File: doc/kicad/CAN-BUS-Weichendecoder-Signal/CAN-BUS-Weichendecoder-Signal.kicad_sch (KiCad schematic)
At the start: 26 parts, among them J1 Conn_01x04_Male, J1001 Wago 250-1406, J11 250-1406, J12 Wago 250-1406, J13 Wago 250-1406, J14 Wago 250-1406, J15 Wago 250-1406, J21 Conn_01x06, J22 Conn_01x06, U1 PCF8574, U2 PCF8574, U3 PCF8574, U4 PCF8574, U5 ULN2803A, U6 ULN2803A, U7 ULN2803A, U8 ULN2803A

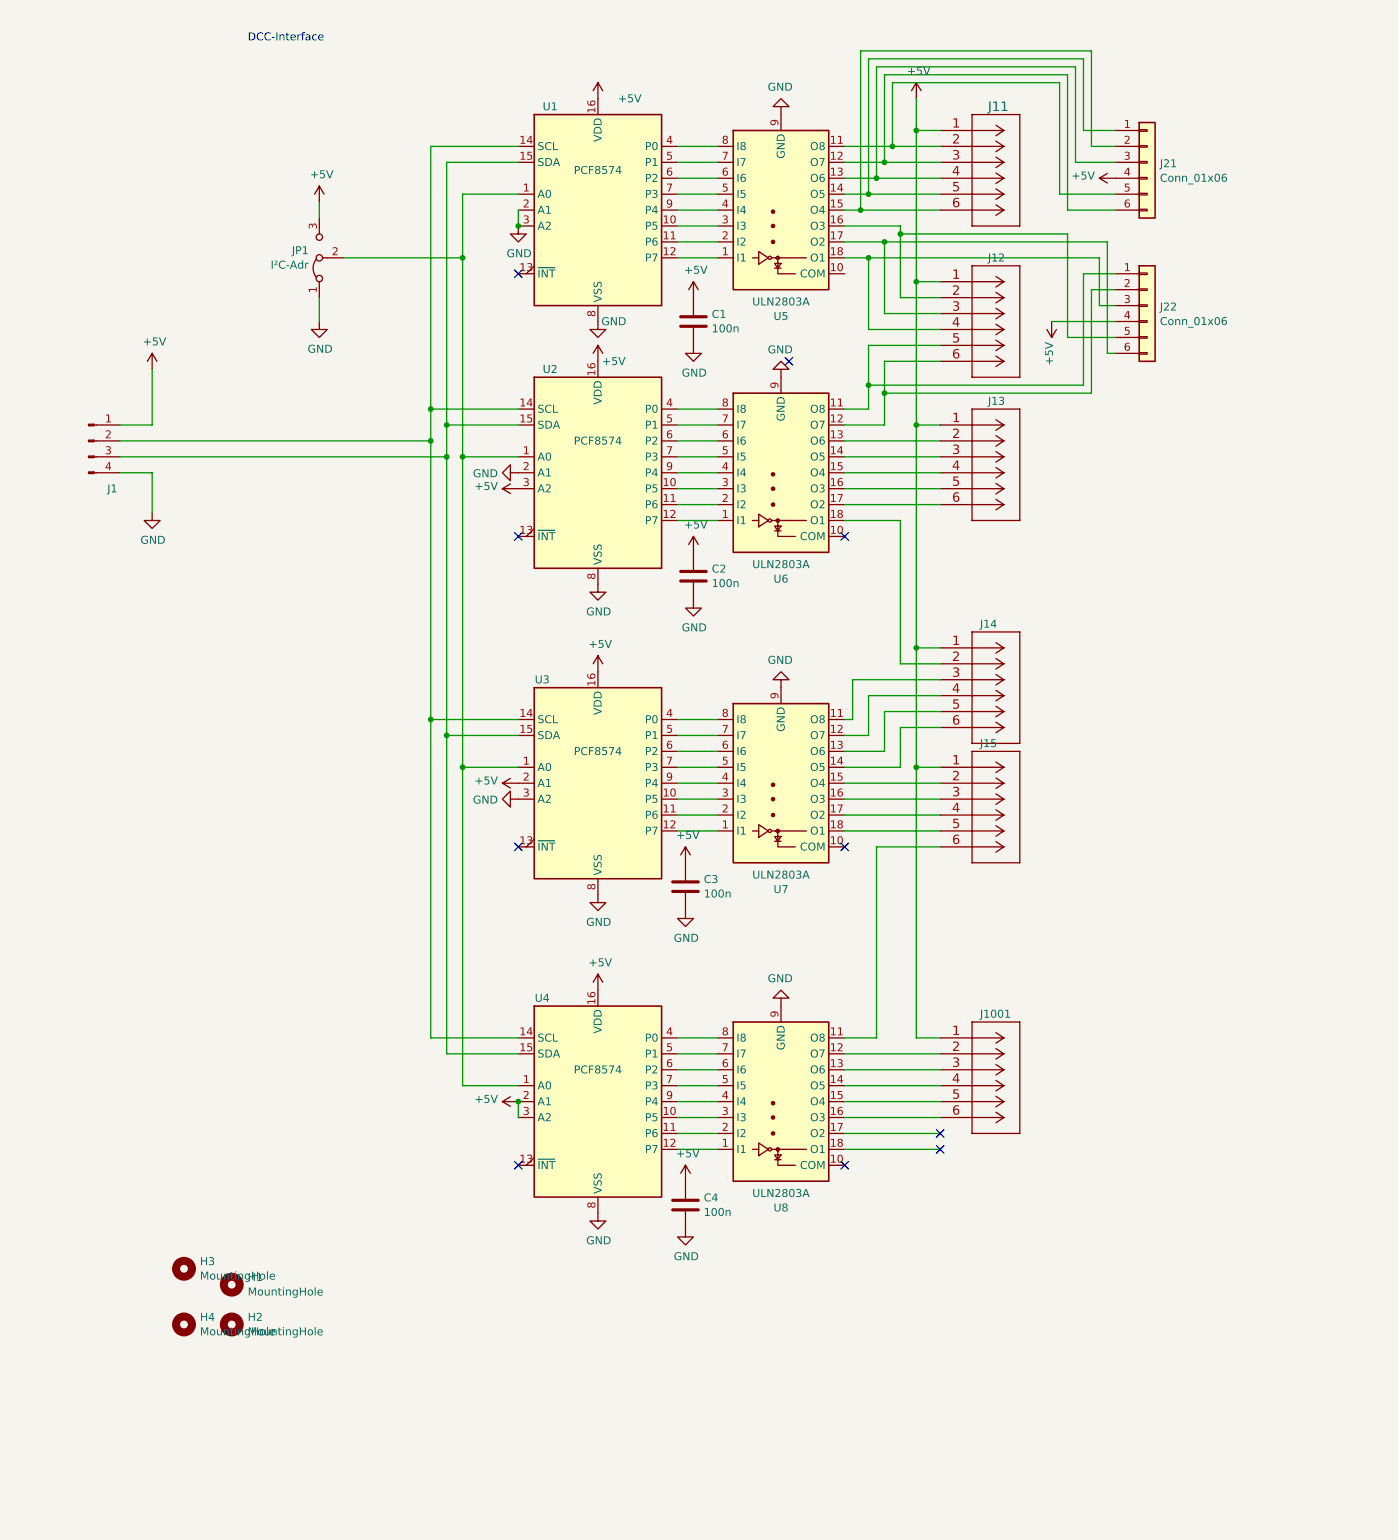
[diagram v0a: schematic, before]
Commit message: RJ12 hinzugefügt
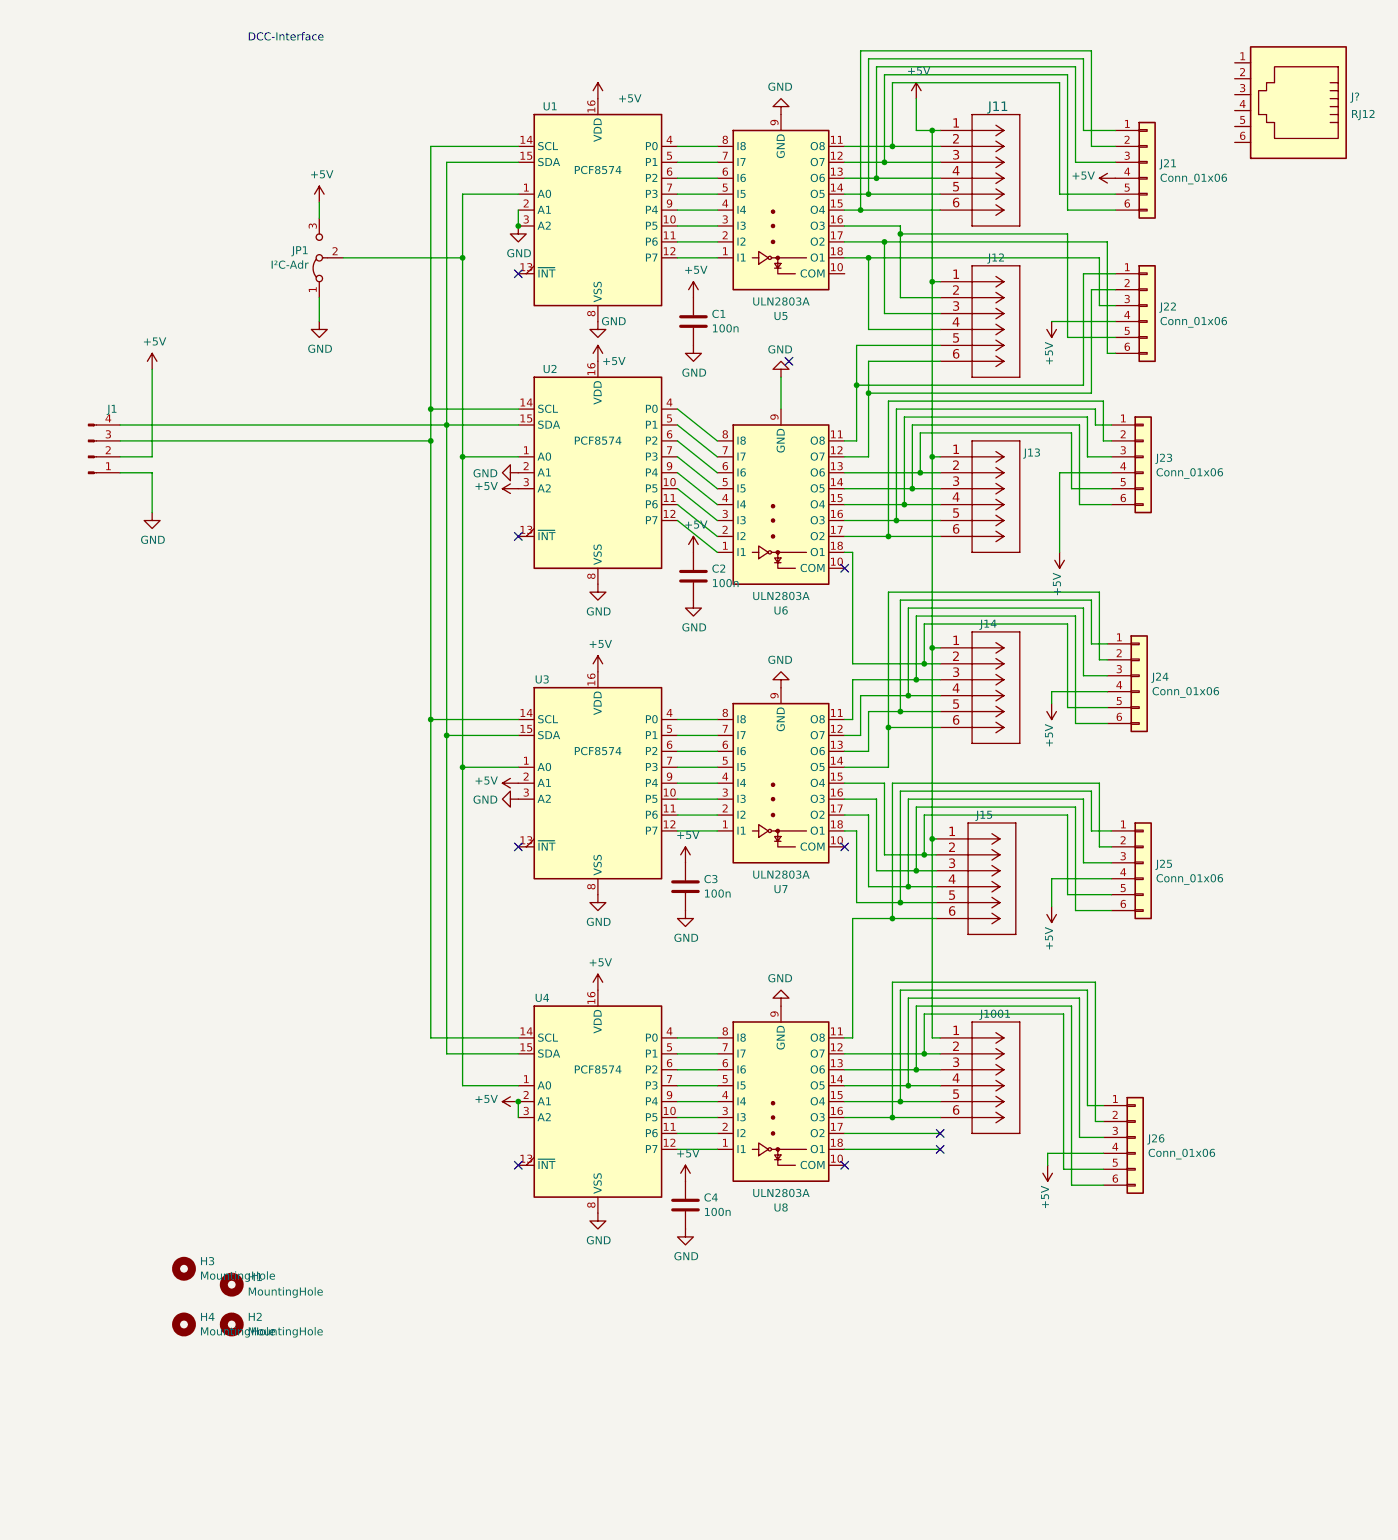
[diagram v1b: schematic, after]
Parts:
- added J23, J24, J25, J26: Conn_01x06, Connector_IDC:IDC-Header_2x03_P2.54mm_Vertical, symbol Connector_Generic:Conn_01x06
- added J?: RJ12, Connector_RJ:RJ12_Amphenol_54601, symbol Connector:RJ12
- J21, J22: footprint Connectors_IDC:IDC-Header_2x03_P2.54mm_Vertical -> Connector_IDC:IDC-Header_2x03_P2.54mm_Vertical
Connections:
- net +5V: now also J1.2 (Pin_2), J23.4 (Pin_4), J24.4 (Pin_4), J25.4 (Pin_4), J26.4 (Pin_4); no longer J1.1 (Pin_1)
- net GND: now also J1.1 (Pin_1); no longer J1.4 (Pin_4)
- net at U1.14 (SCL), U2.14 (SCL), U3.14 (SCL)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: now also J1.3 (Pin_3); no longer J1.2 (Pin_2)
- net at U1.15 (SDA), U2.15 (SDA), U3.15 (SDA)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: now also J1.4 (Pin_4); no longer J1.3 (Pin_3)
- net at J13.2, U6.13 (O6): now also J23.5 (Pin_5)
- net at J13.3, U6.14 (O5): now also J23.6 (Pin_6)
- net at J13.4, U6.15 (O4): now also J23.3 (Pin_3)
- net at J13.5, U6.16 (O3): now also J23.1 (Pin_1)
- net at J13.6, U6.17 (O2): now also J23.2 (Pin_2)
- net at J14.2, U6.18 (O1): now also J24.5 (Pin_5)
- net at J14.3, U7.11 (O8): now also J24.6 (Pin_6)
- net at J14.4, U7.12 (O7): now also J24.3 (Pin_3)
- net at J14.5, U7.13 (O6): now also J24.1 (Pin_1)
- net at J14.6, U7.14 (O5): now also J24.2 (Pin_2)
- net at J15.2, U7.15 (O4): now also J25.5 (Pin_5)
- net at J15.3, U7.16 (O3): now also J25.6 (Pin_6)
- net at J15.4, U7.17 (O2): now also J25.3 (Pin_3)
- net at J15.5, U7.18 (O1): now also J25.1 (Pin_1)
- net at J15.6, U8.11 (O8): now also J25.2 (Pin_2)
- net at J1001.2, U8.12 (O7): now also J26.5 (Pin_5)
- net at J1001.3, U8.13 (O6): now also J26.6 (Pin_6)
- net at J1001.4, U8.14 (O5): now also J26.3 (Pin_3)
- net at J1001.5, U8.15 (O4): now also J26.1 (Pin_1)
- net at J1001.6, U8.16 (O3): now also J26.2 (Pin_2)
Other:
- moved on the sheet: J13, J15, U6

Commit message: Ausgänge in zwei Blöcke aufgetreilt, Ausgangsspannung kann extern eingespeist werden
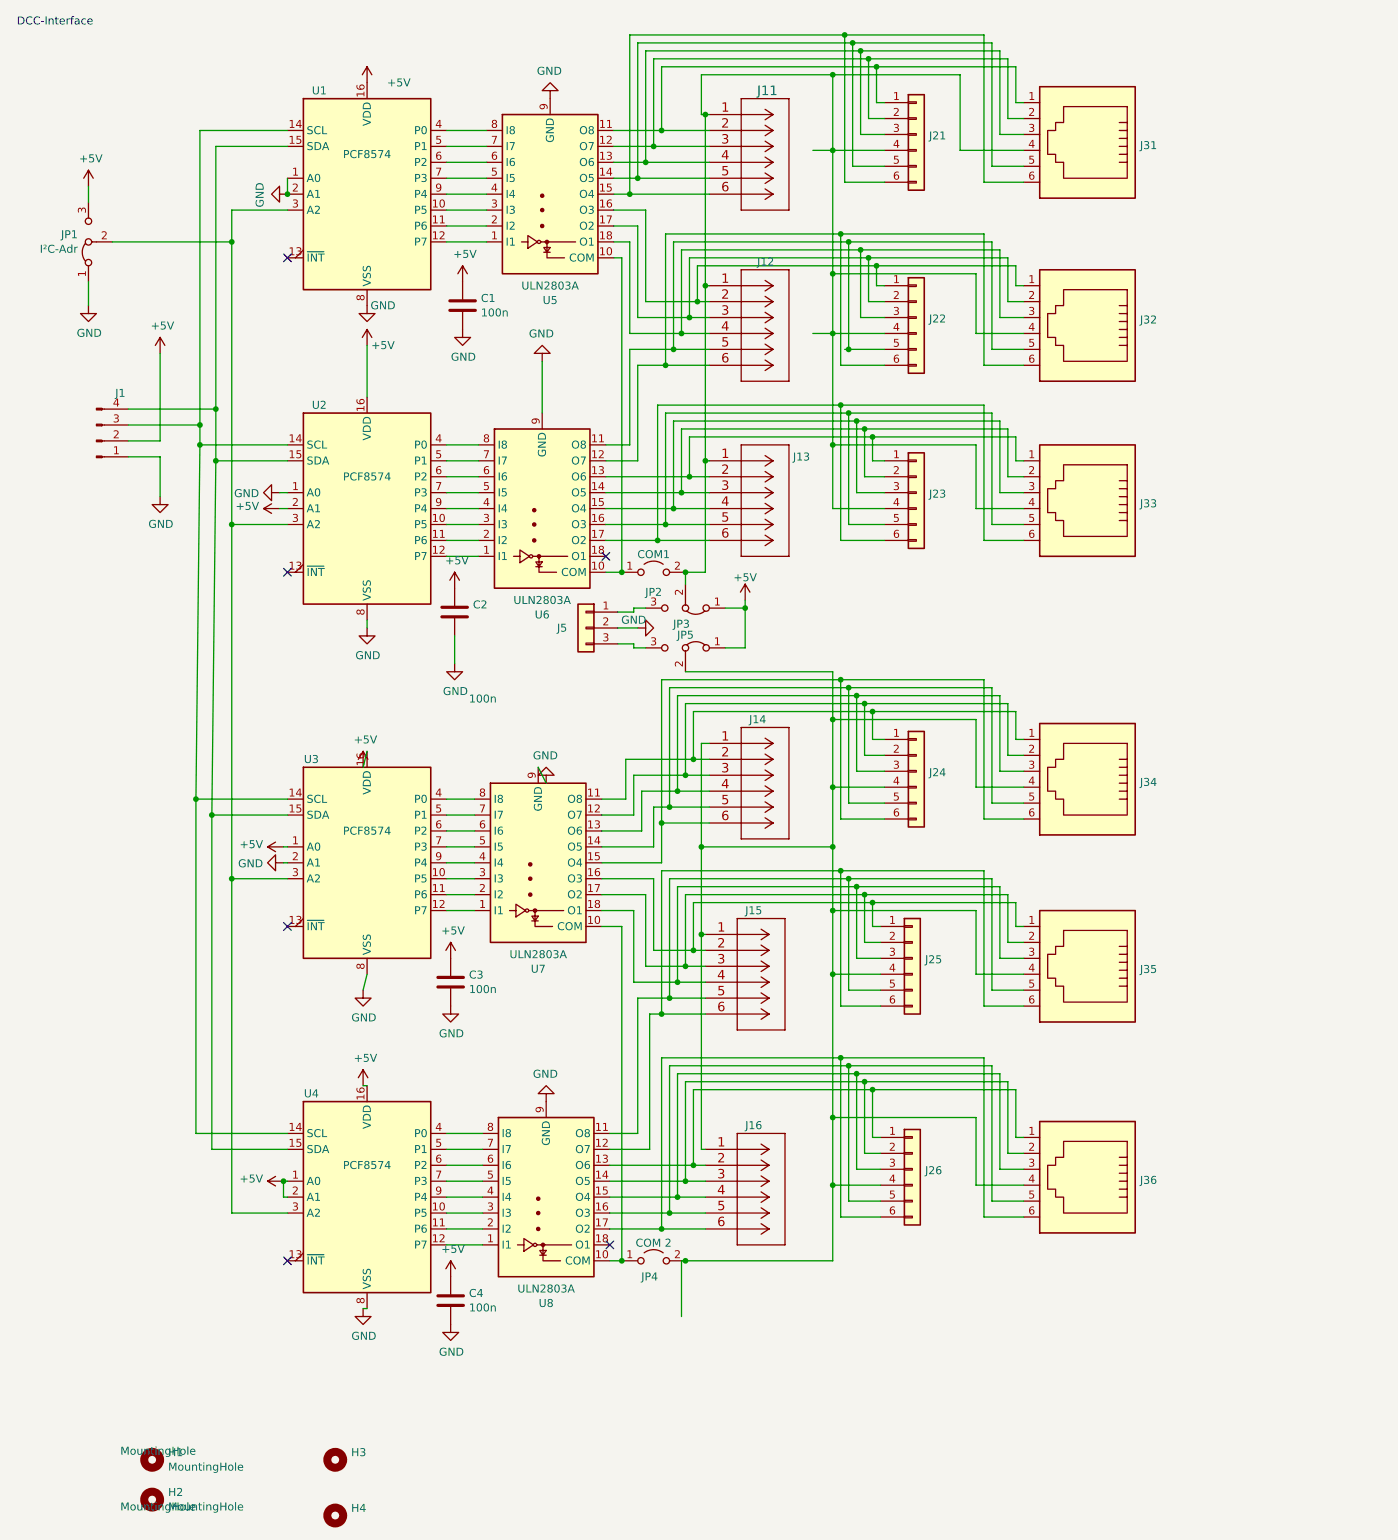
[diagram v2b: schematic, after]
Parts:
- added J31, J32, J34, J35, J36: RJ12, Connector_RJ:RJ12_Amphenol_54601, symbol Connector:RJ12
- added J5: Conn_01x03, TerminalBlock:TerminalBlock_bornier-3_P5.08mm, symbol Connector_Generic:Conn_01x03
- added JP2: COM1, Connector_PinHeader_2.54mm:PinHeader_1x02_P2.54mm_Vertical, symbol Jumper:Jumper_2_Open
- added JP3, JP5: Jumper_3_Bridged12, Connector_PinHeader_2.54mm:PinHeader_1x03_P2.54mm_Vertical, symbol Jumper:Jumper_3_Bridged12
- added JP4: COM 2, Connector_PinHeader_2.54mm:PinHeader_1x02_P2.54mm_Vertical, symbol Jumper:Jumper_2_Open
- gave numbers to parts that had none: 1
- renumbered J1001 to J16
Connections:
- net +5V: now also U2.2 (A1), U3.1 (A0), U4.1 (A0), JP3.1 (A), JP5.1 (A); no longer J11.1, J12.1, J13.1, J14.1, J15.1, J16.1, J21.4 (Pin_4), J22.4 (Pin_4), J23.4 (Pin_4), J24.4 (Pin_4), J25.4 (Pin_4), J26.4 (Pin_4), U2.3 (A2), U3.2 (A1), U4.3 (A2)
- net GND: now also U1.1 (A0), U2.1 (A0), U3.2 (A1), J5.2 (Pin_2); no longer U1.3 (A2), U2.2 (A1), U3.3 (A2)
- net at U5.10 (COM): now also U6.10 (COM), JP2.1 (A)
- net at J11.2, U5.11 (O8): now also J21.1 (Pin_1), J31.1; no longer J21.5 (Pin_5)
- net at J11.3, U5.12 (O7): now also J21.2 (Pin_2), J31.2; no longer J21.6 (Pin_6)
- net at J11.4, J21.3 (Pin_3), U5.13 (O6): now also J31.3
- net at J11.5, U5.14 (O5): now also J21.5 (Pin_5), J31.5; no longer J21.1 (Pin_1)
- net at J11.6, U5.15 (O4): now also J21.6 (Pin_6), J31.6; no longer J21.2 (Pin_2)
- net at J12.2, U5.16 (O3): now also J22.1 (Pin_1), J32.1; no longer J22.5 (Pin_5)
- net at J12.3, U5.17 (O2): now also J22.2 (Pin_2), J32.2; no longer J22.6 (Pin_6)
- net at J12.4, J22.3 (Pin_3), U5.18 (O1): now also J32.3
- net at J12.5, U6.11 (O8): now also J22.5 (Pin_5), J32.5; no longer J22.1 (Pin_1)
- net at J12.6, U6.12 (O7): now also J22.6 (Pin_6), J32.6; no longer J22.2 (Pin_2)
- net at J13.2, U6.13 (O6): now also J23.1 (Pin_1), J33.1; no longer J23.5 (Pin_5)
- net at J13.3, U6.14 (O5): now also J23.2 (Pin_2), J33.2; no longer J23.6 (Pin_6)
- net at J13.4, J23.3 (Pin_3), U6.15 (O4): now also J33.3
- net at J13.5, U6.16 (O3): now also J23.5 (Pin_5), J33.5; no longer J23.1 (Pin_1)
- net at J13.6, U6.17 (O2): now also J23.6 (Pin_6), J33.6; no longer J23.2 (Pin_2)
- net at U7.10 (COM): now also U8.10 (COM), JP4.1 (A)
- net at J14.4, J24.3 (Pin_3): now also U7.13 (O6), J34.3; no longer U7.12 (O7)
- net at J15.4, J25.3 (Pin_3): now also U7.18 (O1), J35.3; no longer U7.17 (O2)
- net at J16.4, J26.3 (Pin_3): now also U8.15 (O4), J36.3; no longer U8.14 (O5)
- net at U8.17 (O2): now also J16.6, J26.6 (Pin_6), J36.6
- net at J33.4: now also J11.1, J12.1, J13.1, J21.4 (Pin_4), J22.4 (Pin_4), J23.4 (Pin_4), J31.4, J32.4, JP2.2 (B), JP3.2 (C)
- new net: JP1.2 (C), U1.3 (A2), U2.3 (A2), U3.3 (A2), U4.3 (A2)
- new net: J14.2, J24.1 (Pin_1), J34.1, U7.11 (O8)
- new net: J14.3, J24.2 (Pin_2), J34.2, U7.12 (O7)
- new net: J14.5, J24.5 (Pin_5), J34.5, U7.14 (O5)
- new net: J14.6, J24.6 (Pin_6), J34.6, U7.15 (O4)
- new net: J15.2, J25.1 (Pin_1), J35.1, U7.16 (O3)
- new net: J15.3, J25.2 (Pin_2), J35.2, U7.17 (O2)
- new net: J14.1, J15.1, J16.1, J24.4 (Pin_4), J25.4 (Pin_4), J26.4 (Pin_4), J34.4, J35.4, J36.4, JP4.2 (B), JP5.2 (C)
- new net: J15.5, J25.5 (Pin_5), J35.5, U8.11 (O8)
- new net: J15.6, J25.6 (Pin_6), J35.6, U8.12 (O7)
- new net: J16.2, J26.1 (Pin_1), J36.1, U8.13 (O6)
- new net: J16.3, J26.2 (Pin_2), J36.2, U8.14 (O5)
- new net: J16.5, J26.5 (Pin_5), J36.5, U8.16 (O3)
- new net: J5.1 (Pin_1), JP3.3 (B)
- new net: J5.3 (Pin_3), JP5.3 (B)
- now unconnected: U6.18 (O1)
- no-connect marks 10 -> 6
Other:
- moved on the sheet: C1, C2, C3, C4, H1, H2, H3, H4, J1, J11, J12, J13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

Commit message: Beschriftung hinzugefügt
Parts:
- J11, J12, J13, J14, J15, J16: footprint Wago:CONN_250-1406_WAG -> Wago:CONN_250-1406_WAG_Light
- J21, J22, J23, J24, J25, J26: footprint Connector_IDC:IDC-Header_2x03_P2.54mm_Vertical -> Wago:IDC-Header_2x03_P2.54mm_Vertical_Light
- J31, J32, J33, J34, J35, J36: footprint Connector_RJ:RJ12_Amphenol_54601 -> Wago:RJ12_Amphenol_54601_Light
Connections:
- net SCL: now reaches J1.3 (Pin_3), U1.14 (SCL), U2.14 (SCL), U3.14 (SCL), U4.14 (SCL)
